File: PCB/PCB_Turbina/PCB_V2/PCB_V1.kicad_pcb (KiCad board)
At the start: 2 copper layers, 194 x 80 mm, 13 parts, among them J1 BATT_11.1V, J2 Conn_01x07, J3 ENODER_LEFT, J4 ENODER_RIGH, J5 BATT_7.4V, J6 JST-7.7V, J7 TURBINE_POWER, J8 TURBINE_PWM, SW1 Switch, U1 WeMos_S2_mini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

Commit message: Correccion Agujeros 3mm
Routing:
- net GND: track 547.9 -> 564.7 mm, vias 2 -> 4

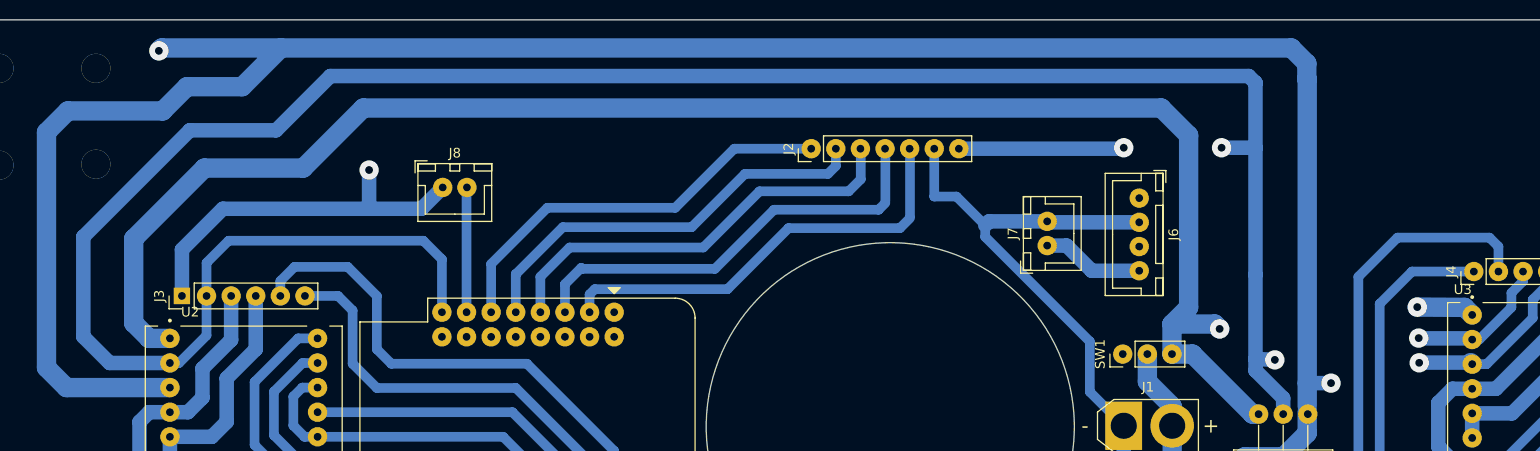
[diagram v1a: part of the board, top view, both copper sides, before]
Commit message: Correccion modulo arranque PCB
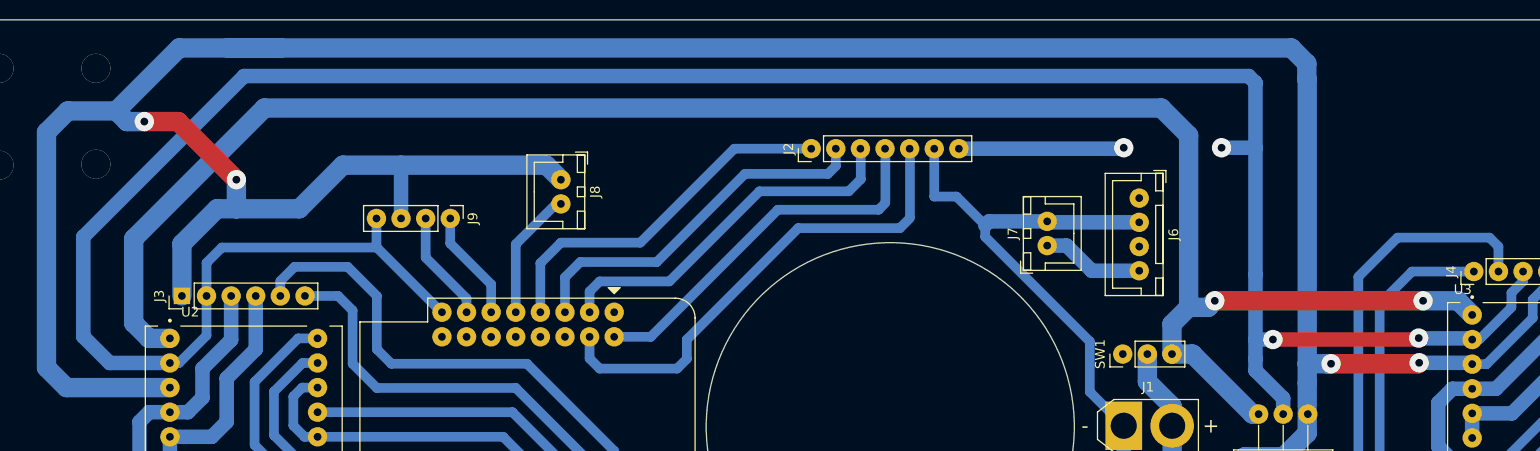
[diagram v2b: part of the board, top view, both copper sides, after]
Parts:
- added J9: Modulo de arranque, Connector_PinHeader_2.54mm:PinHeader_1x04_P2.54mm_Vertical, F.Cu at (109.6, 80.5)
- moved J8 12.2 mm to (121.0, 76.5), turned to -90 degrees
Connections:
- U1 pad 17: unconnected-(U1-GPIO1-Pad17) -> MUX1
- U1 pad 18: unconnected-(U1-GPIO2-Pad18) -> ADC
- U1 pad 2: ADC -> MUX2
- U1 pad 3: MUX1 -> MUX3
- U1 pad 4: MUX2 -> MUX4
- U1 pad 5: MUX3 -> PWM_TURBINE
- U1 pad 6: MUX4 -> Stop
- U1 pad 7: PWM_TURBINE -> Start
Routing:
- net GND: track 564.7 -> 600.9 mm
- net BATT: track 175.0 -> 193.9 mm
- net +3.3V: track 266.3 -> 280.3 mm
- net Stop: track 0.00 -> 11.4 mm
- net Start: track 0.00 -> 11.4 mm
- net MUX2: track 44.0 -> 38.0 mm
- net MUX1: track 44.8 -> 39.0 mm
- net MUX3: track 43.4 -> 38.1 mm
- net ADC: track 45.0 -> 50.2 mm
- net MUX4: track 42.9 -> 37.9 mm
- net PWM_TURBINE: track 12.9 -> 13.4 mm

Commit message: PCB_V3
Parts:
- removed U4: LM1117T-3.3, Package_TO_SOT_THT:TO-220-3_Horizontal_TabDown
- added J10: Conn_01x04, Connector_PinHeader_2.54mm:PinHeader_1x04_P2.54mm_Vertical, F.Cu at (97.1, 84.0)
- J9: value Modulo de arranque -> Conn_01x03; footprint Connector_PinHeader_2.54mm:PinHeader_1x04_P2.54mm_Vertical -> Connector_PinHeader_2.54mm:PinHeader_1x03_P2.54mm_Vertical
- moved J9 104.4 mm to (209.5, 110.8)
- moved J8 70.3 mm to (182.5, 110.5), turned to 180 degrees
- moved J4 62.7 mm to (180.2, 138.0)
- moved J3 59.4 mm to (114.8, 138.0)
- moved U3 43.1 mm to (188.9, 126.1), turned to 90 degrees
- moved U2 40.9 mm to (121.1, 126.1), turned to 90 degrees
- moved J2 38.8 mm to (109.5, 84.0)
- moved J7 35.7 mm to (194.2, 110.5), turned to 180 degrees
- moved J6 29.8 mm to (199.2, 101.8), turned to 180 degrees
- moved J5 19.3 mm to (180.0, 91.0)
- moved SW1 13.7 mm to (192.5, 92.0)
- moved U1 3.03 mm to (124.7, 87.8)
- moved J1 1.20 mm to (178.8, 100.8)
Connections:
- J3 pad 1: GND -> +3.3V
- J3 pad 2: +3.3V -> GND
- J4 pad 1: OUTB_RIGH -> OUTA_RIGH
- J4 pad 2: OUTA_RIGH -> OUTB_RIGH
- J4 pad 4: GND -> M2_RIGH
- J4 pad 6: M2_RIGH -> GND
- J6 pad 1: unconnected-(J6-Pin_1-Pad1) -> GND
- J6 pad 2: GND -> unconnected-(J6-Pin_2-Pad2)
- J6 pad 3: unconnected-(J6-Pin_3-Pad3) -> 7.4V
- J6 pad 4: 7.4V -> unconnected-(J6-Pin_4-Pad4)
- J9 pad 1: Stop -> GND
- J9 pad 2: Start -> +3.3V
- U1 pad 11: PWM_RIGH -> OUTB_LEFT
- U1 pad 12: IN2_RIGH -> OUTA_LEFT
- U1 pad 13: IN1_RIGH -> PWM_LEFT
- U1 pad 14: STBY_RIGH -> IN2_LEFT
- U1 pad 15: OUTB_RIGH -> IN1_LEFT
- U1 pad 16: OUTA_RIGH -> STBY_LEFT
- U1 pad 17: MUX1 -> unconnected-(U1-GPIO1-Pad17)
- U1 pad 18: ADC -> unconnected-(U1-GPIO2-Pad18)
- U1 pad 2: MUX2 -> unconnected-(U1-GPIO3-Pad2)
- U1 pad 23: unconnected-(U1-GPIO13-Pad23) -> START
- U1 pad 24: unconnected-(U1-GPIO14-Pad24) -> STOP
- U1 pad 25: unconnected-(U1-XTAL_32K_P-Pad25) -> PWM_TURBINE
- U1 pad 27: PWM_LEFT -> PWM_RIGH
- U1 pad 28: IN2_LEFT -> IN2_RIGH
- U1 pad 29: IN1_LEFT -> IN1_RIGH
- U1 pad 3: MUX3 -> ADC
- U1 pad 30: STBY_LEFT -> STBY_RIGH
- U1 pad 31: OUTA_LEFT -> OUTB_RIGH
- U1 pad 32: OUTB_LEFT -> OUTA_RIGH
- U1 pad 4: MUX4 -> MUX1
- U1 pad 5: PWM_TURBINE -> MUX2
- U1 pad 6: Stop -> MUX3
- U1 pad 7: Start -> MUX4
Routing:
- net GND: track 600.9 -> 0.00 mm, vias 4 -> 0
- net PWM_TURBINE: track 13.4 -> 96.8 mm
- net PWM_RIGH: track 171.0 -> 108.4 mm
- net IN2_RIGH: track 157.9 -> 100.7 mm
- net OUTA_RIGH: track 126.1 -> 69.7 mm
- net BATT: track 193.9 -> 137.8 mm
- net IN1_RIGH: track 145.6 -> 93.4 mm
- net OUTB_RIGH: track 126.2 -> 78.3 mm
- net ADC: track 50.2 -> 3.81 mm
- net STBY_RIGH: track 131.1 -> 85.4 mm
- net MUX1: track 39.0 -> 3.81 mm
- net MUX3: track 38.1 -> 3.81 mm
- net MUX2: track 38.0 -> 3.81 mm
- net MUX4: track 37.9 -> 3.81 mm
- net STBY_LEFT: track 32.4 -> 9.63 mm
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- added copper zone on B.Cu, net GND
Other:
- board size 194 x 80 mm -> 150 x 59.8 mm
